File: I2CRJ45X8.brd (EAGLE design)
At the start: 80 x 50 mm, 51 parts, among them IC1 MCP23017SO, IC2 MCP23017SO, J1 M06-SOCKET, J2 M06-SOCKET, J3 M02X3-PIN, J4 M02X3-PIN

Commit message: Part updates
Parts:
- renumbered U$1 to J5

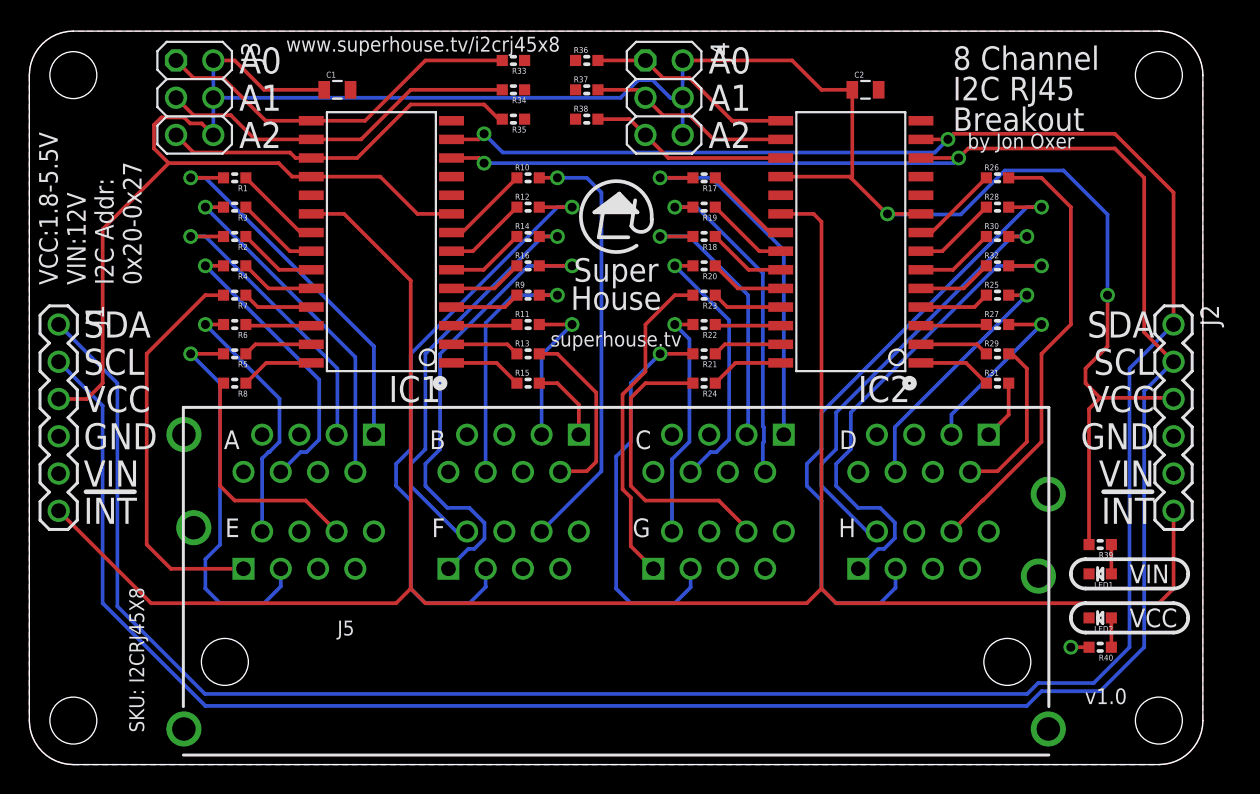
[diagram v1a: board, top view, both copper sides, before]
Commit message: Added fiducials
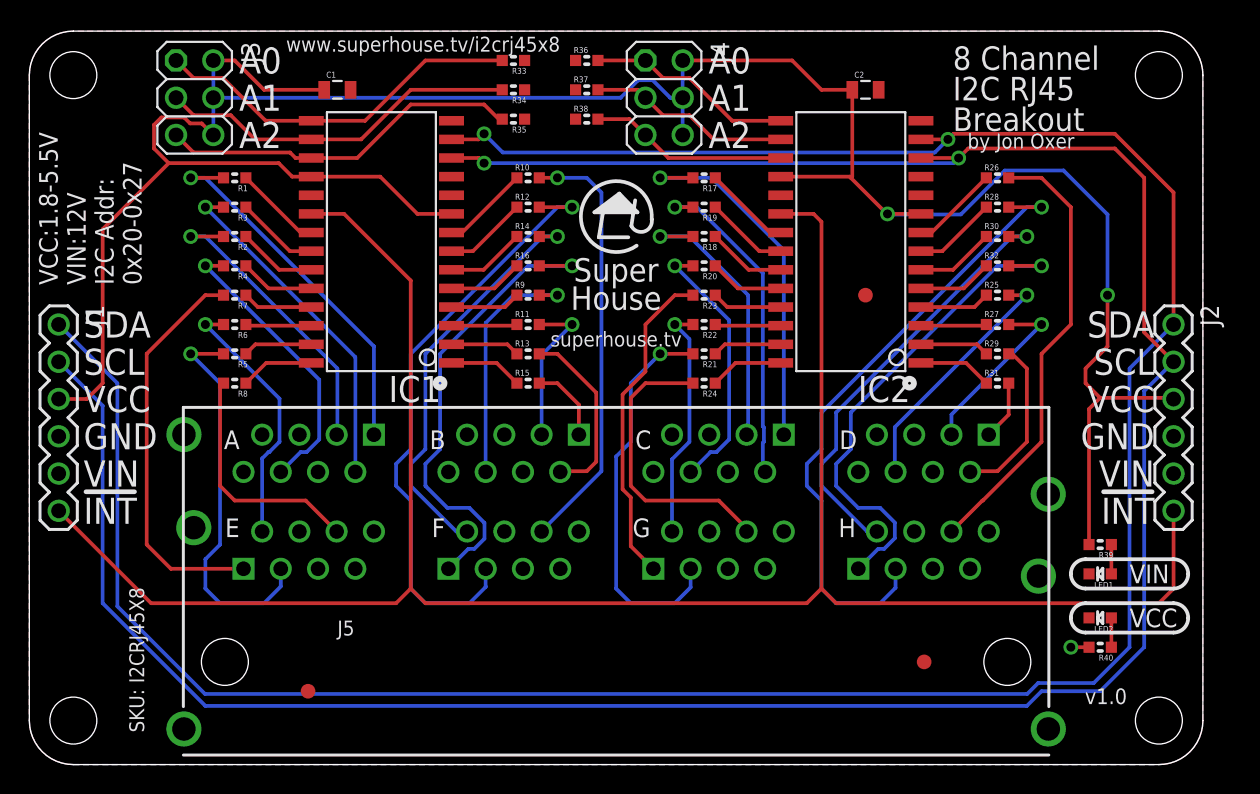
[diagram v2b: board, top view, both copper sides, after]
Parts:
- added FID1, FID2, FID3: FIDUCIAL1X2.5, freetronics:FIDUCIAL-1X2.5
